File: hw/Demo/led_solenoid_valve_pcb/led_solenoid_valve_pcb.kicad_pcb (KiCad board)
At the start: 2 copper layers, 3 parts, among them J1 Conn_01x02

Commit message: FINAL REVIEW DONE + A lot of fixes. DRC PASSED
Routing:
- added copper zone on B.Cu, net (none)
- added copper zone on F.Cu, net (none)
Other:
- board outline added: 7.5 x 7.5 mm
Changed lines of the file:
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@@
 		(capping no)
 		(filling no)
-		(zone_defaults)
+		(zone_defaults
+			(property
+				(layer "In1.Cu")
+				(hatch_position
+					(xy 0 0)
+				)
+			)
+		)
 		(pcbplotparams
 			(layerselection 0x00000000_00000000_55555555_5755f5ff)
@@
 		(tags "Through hole pin header THT 1x02 2.54mm single row")
 		(property "Reference" "J1"
-			(at 2.58 -1.235 180)
+			(at 2.58 -1.235 0)
 			(layer "F.SilkS")
 			(effects
@@
 		(embedded_fonts no)
 		(model "${KICAD10_3DMODEL_DIR}/Connector_PinHeader_2.54mm.3dshapes/PinHeader_1x02_P2.54mm_Vertical.step"
+			(hide yes)
 			(offset
 				(xyz 0 0 0)
@@
 		)
 	)
+	(gr_line
+		(start 51.75 22.75)
+		(end 51.75 27.25)
+		(stroke
+			(width 0.05)
+			(type default)
+		)
+		(layer "Edge.Cuts")
+	)
 	(gr_arc
-		(start 51.685 22.77)
-		(mid 52.125804 21.705804)
-		(end 53.19 21.265)
+		(start 51.75 22.75)
+		(mid 52.18934 21.68934)
+		(end 53.25 21.25)
 		(stroke
-			(width 0.1)
+			(width 0.05)
 			(type default)
 		)
-		(layer "F.Paste")
+		(layer "Edge.Cuts")
+	)
+	(gr_arc
+		(start 53.25 28.75)
+		(mid 52.18934 28.31066)
+		(end 51.75 27.25)
+		(stroke
+			(width 0.05)
+			(type default)
+		)
+		(layer "Edge.Cuts")
 	)
 	(gr_line
-		(start 51.685002 22.771687)
-		(end 51.690002 27.231682)
+		(start 53.25 28.75)
+		(end 57.75 28.75)
 		(stroke
-			(width 0.1)
+			(width 0.05)
 			(type default)
 		)
-		(layer "F.Paste")
+		(layer "Edge.Cuts")
+	)
+	(gr_line
+		(start 57.75 21.25)
+		(end 53.25 21.25)
+		(stroke
+			(width 0.05)
+			(type default)
+		)
+		(layer "Edge.Cuts")
 	)
 	(gr_arc
-		(start 53.19 28.73)
-		(mid 52.12934 28.29066)
-		(end 51.69 27.23)
+		(start 57.75 21.25)
+		(mid 58.81066 21.68934)
+		(end 59.25 22.75)
 		(stroke
-			(width 0.1)
+			(width 0.05)
 			(type default)
 		)
-		(layer "F.Paste")
+		(layer "Edge.Cuts")
+	)
+	(gr_arc
+		(start 59.25 27.25)
+		(mid 58.81066 28.31066)
+		(end 57.75 28.75)
+		(stroke
+			(width 0.05)
+			(type default)
+		)
+		(layer "Edge.Cuts")
 	)
 	(gr_line
-		(start 53.191606 28.729998)
-		(end 57.861601 28.724998)
+		(start 59.25 27.25)
+		(end 59.25 22.75)
 		(stroke
-			(width 0.1)
+			(width 0.05)
 			(type default)
 		)
-		(layer "F.Paste")
-	)
-	(gr_arc
-		(start 57.85 21.27)
-		(mid 58.91066 21.70934)
-		(end 59.35 22.77)
-		(stroke
-			(width 0.1)
-			(type default)
-		)
-		(layer "F.Paste")
-	)
-	(gr_line
-		(start 57.851609 21.270002)
-		(end 53.191615 21.265002)
-		(stroke
-			(width 0.1)
-			(type default)
-		)
-		(layer "F.Paste")
-	)
-	(gr_arc
-		(start 59.355 27.23)
-		(mid 58.917125 28.287125)
-		(end 57.86 28.725)
-		(stroke
-			(width 0.1)
-			(type default)
-		)
-		(layer "F.Paste")
-	)
-	(gr_line
-		(start 59.355 27.23)
-		(end 59.35 22.77)
-		(stroke
-			(width 0.1)
-			(type default)
-		)
-		(layer "F.Paste")
+		(layer "Edge.Cuts")
 	)
 	(gr_text "mm\n"
@@
 		)
 	)
-	(dimension
-		(type orthogonal)
-		(layer "Edge.Cuts")
-		(pts
-			(xy 59.38 25.84) (xy 51.72 25.88)
-		)
-		(height 6.44)
-		(orientation 0)
-		(format
-			(prefix "")
-			(suffix "")
-			(units 3)
-			(units_format 0)
-			(precision 4)
-			(suppress_zeroes yes)
-		)
-		(style
-			(thickness 0.05)
-			(arrow_length 1.27)
-			(text_position_mode 0)
-			(arrow_direction outward)
-			(extension_height 0.58642)
-			(extension_offset 0.5)
-			(keep_text_aligned yes)
-		)
-		(gr_text "7.66"
-			(at 55.55 31.13 0)
-			(layer "Edge.Cuts")
-			(effects
-				(font
-					(size 1 1)
-					(thickness 0.15)
-				)
-			)
-		)
-	)
-	(dimension
-		(type orthogonal)
-		(layer "Edge.Cuts")
-		(pts
-			(xy 55.87 28.78) (xy 55.95 21.33)
-		)
-		(height 10.47)
-		(orientation 1)
-		(format
-			(prefix "")
-			(suffix "")
-			(units 3)
-			(units_format 0)
-			(precision 4)
-			(suppress_zeroes yes)
-		)
-		(style
-			(thickness 0.05)
-			(arrow_length 1.27)
-			(text_position_mode 0)
-			(arrow_direction outward)
-			(extension_height 0.58642)
-			(extension_offset 0.5)
-			(keep_text_aligned yes)
-		)
-		(gr_text "7.45"
-			(at 65.19 25.055 90)
-			(layer "Edge.Cuts")
-			(effects
-				(font
-					(size 1 1)
-					(thickness 0.15)
-				)
-			)
-		)
+	(segment
+		(start 56.3975 26.02)
+		(end 56.3975 23.8675)
+		(width 0.5)
+		(layer "F.Cu")
+		(net "Net-(D1-K)")
+	)
+	(segment
+		(start 56.3975 23.8675)
+		(end 56.785 23.48)
+		(width 0.2)
+		(layer "F.Cu")
+		(net "Net-(D1-K)")
 	)
 	(segment
@@
 	)
 	(segment
-		(start 56.3975 26.02)
-		(end 56.3975 23.8675)
-		(width 0.5)
-		(layer "F.Cu")
-		(net "Net-(D1-K)")
-	)
-	(segment
-		(start 56.3975 23.8675)
-		(end 56.785 23.48)
-		(width 0.2)
-		(layer "F.Cu")
-		(net "Net-(D1-K)")
-	)
-	(segment
 		(start 53.395 24.33)
 		(end 54.245 23.48)
@@
 		(net "Net-(J1-Pin_2)")
 	)
+	(zone
+		(layer "F.Cu")
+		(hatch edge 0.5)
+		(connect_pads
+			(clearance 0.5)
+		)
+		(min_thickness 0.25)
+		(fill yes
+			(thermal_gap 0.5)
+			(thermal_bridge_width 0.5)
+			(island_removal_mode 1)
+		)
+		(polygon
+			(pts
+				(xy 60.25 19.5) (xy 60.25 29.5) (xy 50.75 29.5) (xy 50.75 19.5)
+			)
+		)
+	)
+	(zone
+		(layer "B.Cu")
+		(hatch edge 0.5)
+		(priority 1)
+		(connect_pads
+			(clearance 0.5)
+		)
+		(min_thickness 0.25)
+		(fill yes
+			(thermal_gap 0.5)
+			(thermal_bridge_width 0.5)
+			(island_removal_mode 1)
+		)
+		(polygon
+			(pts
+				(xy 60.25 29.5) (xy 60.25 19.5) (xy 50.75 19.5) (xy 50.75 29.5)
+			)
+		)
+	)
 	(embedded_fonts no)

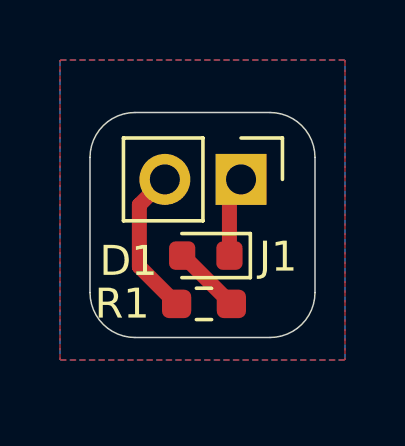
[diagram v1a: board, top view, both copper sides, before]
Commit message: Created Gerbers for PIB / LED Boards + Order Request
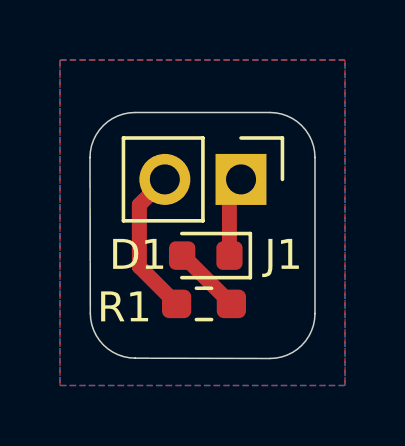
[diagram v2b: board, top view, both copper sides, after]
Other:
- board size 7.5 x 7.5 mm -> 7.5 x 8.2 mm
- board text removed: "mm"
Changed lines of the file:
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@@
 		(capping no)
 		(filling no)
-		(zone_defaults
-			(property
-				(layer "In1.Cu")
-				(hatch_position
-					(xy 0 0)
-				)
-			)
-		)
+		(zone_defaults)
 		(pcbplotparams
 			(layerselection 0x00000000_00000000_55555555_5755f5ff)
@@
 			(outputformat 1)
 			(mirror no)
-			(drillshape 1)
+			(drillshape 0)
 			(scaleselection 1)
-			(outputdirectory "")
+			(outputdirectory "Gerbers/")
 		)
 	)
@@
 		(tags "LED")
 		(property "Reference" "D1"
-			(at 2.5775 -0.18 0)
+			(at 2.26 0.02 0)
 			(layer "F.SilkS")
 			(effects
@@
 		(tags "resistor handsolder")
 		(property "Reference" "R1"
-			(at -2.73 -0.005 0)
+			(at -2.65 0.12 0)
 			(layer "F.SilkS")
 			(effects
@@
 		(tags "Through hole pin header THT 1x02 2.54mm single row")
 		(property "Reference" "J1"
-			(at 2.58 -1.235 0)
+			(at 2.52 -1.415 0)
 			(layer "F.SilkS")
 			(effects
@@
 	(gr_line
 		(start 51.75 22.75)
-		(end 51.75 27.25)
+		(end 51.76066 27.93934)
 		(stroke
 			(width 0.05)
@@
 	)
 	(gr_arc
-		(start 53.25 28.75)
-		(mid 52.18934 28.31066)
-		(end 51.75 27.25)
+		(start 53.26066 29.43934)
+		(mid 52.2 29)
+		(end 51.76066 27.93934)
 		(stroke
 			(width 0.05)
@@
 	)
 	(gr_line
-		(start 53.25 28.75)
-		(end 57.75 28.75)
+		(start 53.26066 29.43934)
+		(end 57.75 29.45)
 		(stroke
 			(width 0.05)
@@
 	)
 	(gr_arc
-		(start 59.25 27.25)
-		(mid 58.81066 28.31066)
-		(end 57.75 28.75)
+		(start 59.25 27.95)
+		(mid 58.81066 29.01066)
+		(end 57.75 29.45)
 		(stroke
 			(width 0.05)
@@
 	)
 	(gr_line
-		(start 59.25 27.25)
+		(start 59.25 27.95)
 		(end 59.25 22.75)
 		(stroke
@@
 		)
 		(layer "Edge.Cuts")
-	)
-	(gr_text "mm\n"
-		(at 67.63 25.8 0)
-		(layer "Edge.Cuts")
-		(effects
-			(font
-				(size 1 1)
-				(thickness 0.15)
-			)
-			(justify left bottom)
-		)
 	)
 	(segment
@@
 		(polygon
 			(pts
-				(xy 60.25 19.5) (xy 60.25 29.5) (xy 50.75 29.5) (xy 50.75 19.5)
+				(xy 60.25 19.5) (xy 60.25 30.35) (xy 50.75 30.35) (xy 50.75 19.5)
 			)
 		)
@@
 		(polygon
 			(pts
-				(xy 60.25 29.5) (xy 60.25 19.5) (xy 50.75 19.5) (xy 50.75 29.5)
-			)
-		)
+				(xy 60.25 30.35) (xy 60.25 19.5) (xy 50.75 19.5) (xy 50.75 30.35)
+			)
+		)
